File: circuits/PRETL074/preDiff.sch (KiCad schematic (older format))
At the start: 56 parts, among them K1 CONN_3, P1 CONN_1, P10 CONN_1, P11 CONN_1, P2 CONN_1, P3 CONN_1, P4 CONN_1, P5 CONN_1, P6 CONN_1, P7 CONN_1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

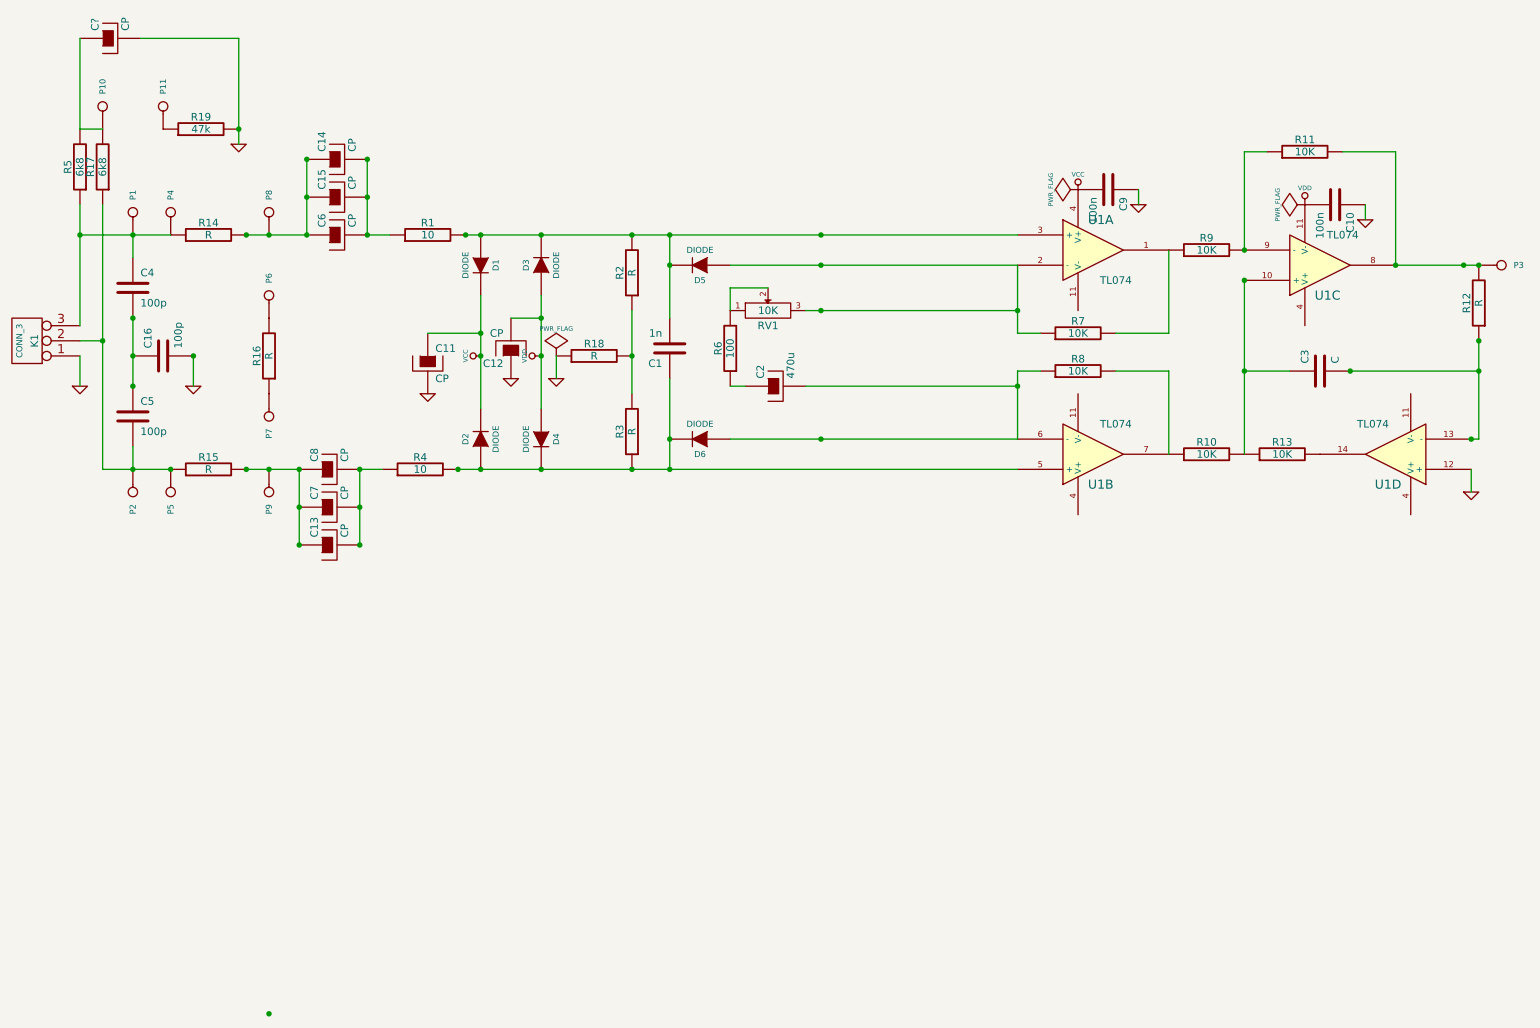
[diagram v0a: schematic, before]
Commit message: docs on transformers
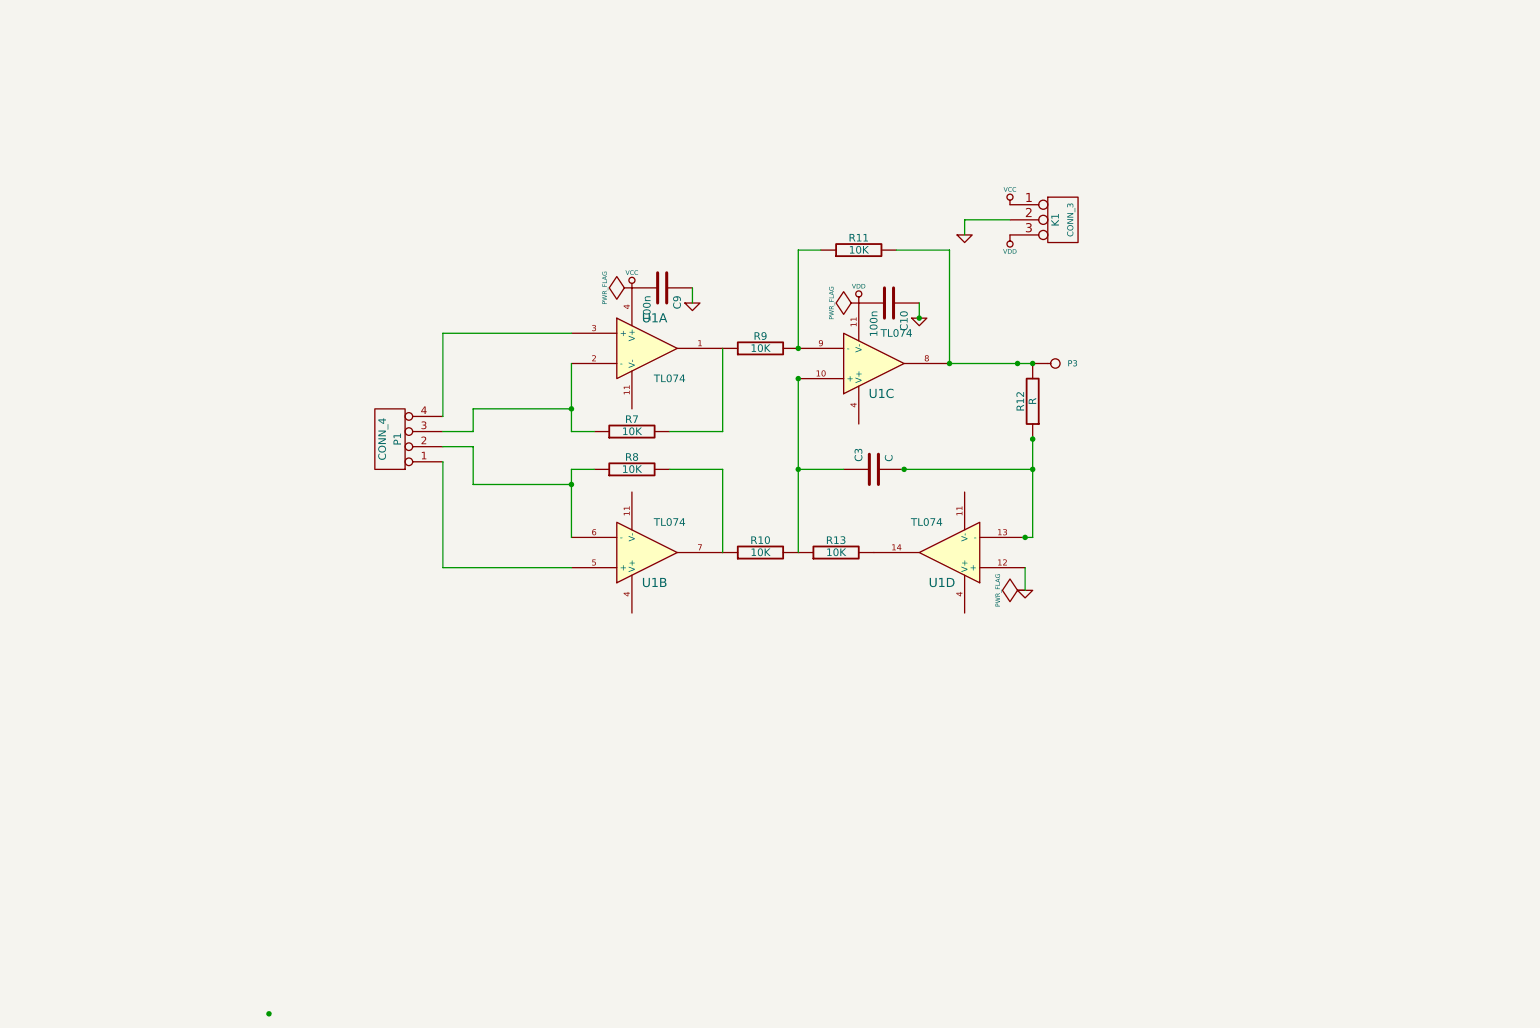
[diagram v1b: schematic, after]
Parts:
- removed C1: 1n, symbol C
- removed C11, C12, C13, C14, C15, C6, C7, C8, C?: CP, symbol CP
- removed C16, C4, C5: 100p, symbol C
- removed C2: 470u, symbol CP
- removed D1, D2, D3, D4, D5, D6: DIODE, symbol DIODE
- removed P1, P10, P11, P2, P4, P5, P6, P7, P8, P9: CONN_1, symbol CONN_1
- removed R1, R4: 10, symbol R
- removed R14, R15, R16, R18, R2, R3: R, symbol R
- removed R17, R5: 6k8, symbol R
- removed R19: 47k, symbol R
- removed R6: 100, symbol R
- removed RV1: 10K, symbol POT
- added P1: CONN_4, symbol CONN_4
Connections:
- net GND: now also K1.2 (PM); no longer K1.1 (P1)
- net VCC: now also K1.1 (P1)
- net VDD: now also K1.3 (P3)
- net at R8.1, U1.6 (-): now also P1.2 (P2)
- net at R7.1, U1.2 (-): now also P1.3 (P3)
- net at U1.5 (+): now also P1.1 (P1)
- net at U1.3 (+): now also P1.4 (P4)
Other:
- moved on the sheet: C10, C3, C9, P3, R10, R11, R12, R13, R7, R8, R9, U1A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
